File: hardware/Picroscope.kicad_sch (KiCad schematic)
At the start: 34 parts, among them J1 USB_C_Receptacle_USB2.0_16P, J2 Conn_01x03_Pin, J3 HDMI_A, J4 Conn_02x09_Odd_Even, U3 AMS1117-3.3

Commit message: added length tuning to 'crucial' traces except qspi
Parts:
- D2: footprint LED_SMD:LED_WS2812B-2020_PLCC4_2.0x2.0mm -> LED_SMD:LED_WS2812B_PLCC4_5.0x5.0mm_P3.2mm
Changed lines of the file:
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@@
 			)
 		)
-		(property "Footprint" "LED_SMD:LED_WS2812B-2020_PLCC4_2.0x2.0mm"
+		(property "Footprint" "LED_SMD:LED_WS2812B_PLCC4_5.0x5.0mm_P3.2mm"
 			(at 87.63 179.07 0)
 			(effects

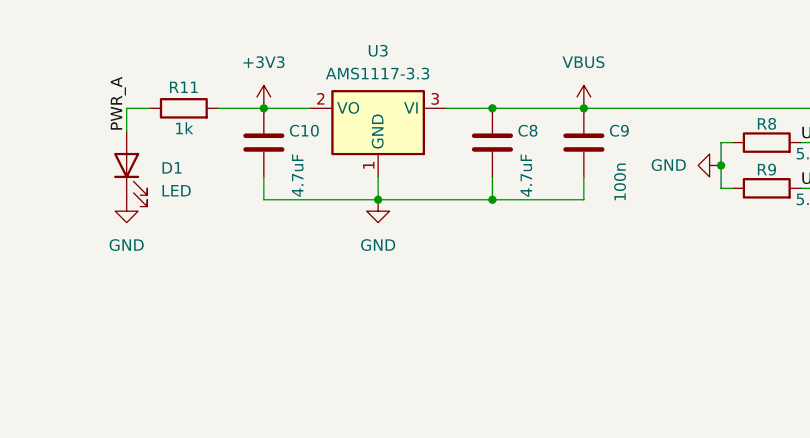
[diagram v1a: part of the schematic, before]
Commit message: changed C8 & C10 to tantalum caps
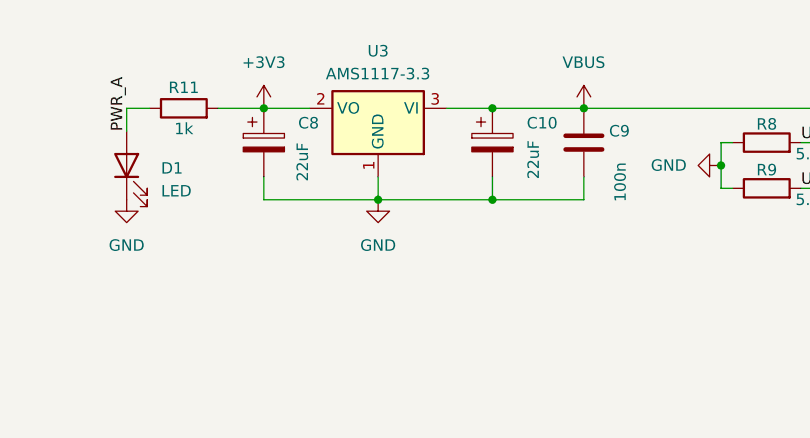
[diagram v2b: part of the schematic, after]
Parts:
- removed C10, C8: 4.7uF, Capacitor_SMD:C_0402_1005Metric, symbol Device:C
- added C10, C8: 22uF, Capacitor_Tantalum_SMD:CP_EIA-3216-18_Kemet-A, symbol Device:C_Polarized
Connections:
- net +3V3: now also C8.1
- net GND: now also C10.2, C8.2
- net VBUS: now also C10.1
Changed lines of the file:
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@@
 	(paper "A4")
 	(junction
-		(at 177.8 30.48)
-		(diameter 0)
-		(color 0 0 0 0)
-	)
-	(junction
 		(at 241.3 96.52)
 		(diameter 0)
@@
 	)
 	(junction
+		(at 177.8 30.48)
+		(diameter 0)
+		(color 0 0 0 0)
+	)
+	(junction
 		(at 39.37 124.46)
 		(diameter 0)
@@
 	(wire
 		(pts
+			(xy 177.8 30.48) (xy 187.96 30.48)
+		)
+		(stroke
+			(width 0)
+			(type default)
+		)
+	)
+	(wire
+		(pts
 			(xy 129.54 104.14) (xy 129.54 105.41)
 		)
@@
 	(wire
 		(pts
-			(xy 177.8 30.48) (xy 187.96 30.48)
-		)
-		(stroke
-			(width 0)
-			(type default)
-		)
-	)
-	(wire
-		(pts
 			(xy 53.34 107.95) (xy 66.04 107.95)
 		)
@@
 	)
 	(symbol
+		(lib_id "Device:C_Polarized")
+		(at 177.8 34.29 0)
+		(unit 1)
+		(exclude_from_sim no)
+		(in_bom yes)
+		(on_board yes)
+		(dnp no)
+		(property "Reference" "C10"
+			(at 181.61 32.1309 0)
+			(effects
+				(font
+					(size 1.27 1.27)
+				)
+				(justify left)
+			)
+		)
+		(property "Value" "22uF"
+			(at 182.372 38.354 90)
+			(effects
+				(font
+					(size 1.27 1.27)
+				)
+				(justify left)
+			)
+		)
+		(property "Footprint" "Capacitor_Tantalum_SMD:CP_EIA-3216-18_Kemet-A"
+			(at 178.7652 38.1 0)
+			(effects
+				(font
+					(size 1.27 1.27)
+				)
+				(hide yes)
+			)
+		)
+		(property "Datasheet" "~"
+			(at 177.8 34.29 0)
+			(effects
+				(font
+					(size 1.27 1.27)
+				)
+				(hide yes)
+			)
+		)
+		(property "Description" "Polarized capacitor"
+			(at 177.8 34.29 0)
+			(effects
+				(font
+					(size 1.27 1.27)
+				)
+				(hide yes)
+			)
+		)
+		(pin "1"
+		)
+		(pin "2"
+		)
+		(instances
+			(project ""
+				(path "/7331d441-a240-49c5-9321-48c59c370619"
+					(reference "C10")
+					(unit 1)
+				)
+			)
+		)
+	)
+	(symbol
 		(lib_id "Mechanical:MountingHole")
 		(at 20.32 166.37 0)
@@
 	)
 	(symbol
-		(lib_id "Device:C")
-		(at 152.4 34.29 0)
-		(unit 1)
-		(exclude_from_sim no)
-		(in_bom yes)
-		(on_board yes)
-		(dnp no)
-		(property "Reference" "C10"
-			(at 155.194 33.02 0)
-			(effects
-				(font
-					(size 1.27 1.27)
-				)
-				(justify left)
-			)
-		)
-		(property "Value" "4.7uF"
-			(at 156.21 40.386 90)
-			(effects
-				(font
-					(size 1.27 1.27)
-				)
-				(justify left)
-			)
-		)
-		(property "Footprint" "Capacitor_SMD:C_0402_1005Metric"
-			(at 153.3652 38.1 0)
-			(effects
-				(font
-					(size 1.27 1.27)
-				)
-				(hide yes)
-			)
-		)
-		(property "Datasheet" "~"
-			(at 152.4 34.29 0)
-			(effects
-				(font
-					(size 1.27 1.27)
-				)
-				(hide yes)
-			)
-		)
-		(property "Description" "Unpolarized capacitor"
-			(at 152.4 34.29 0)
-			(effects
-				(font
-					(size 1.27 1.27)
-				)
-				(hide yes)
-			)
-		)
-		(pin "1"
-		)
-		(pin "2"
-		)
-		(instances
-			(project "Picroscope"
-				(path "/7331d441-a240-49c5-9321-48c59c370619"
-					(reference "C10")
-					(unit 1)
-				)
-			)
-		)
-	)
-	(symbol
 		(lib_id "Connector:TestPoint")
 		(at 220.98 39.37 270)
@@
 	)
 	(symbol
-		(lib_id "Device:C")
-		(at 177.8 34.29 0)
-		(unit 1)
-		(exclude_from_sim no)
-		(in_bom yes)
-		(on_board yes)
-		(dnp no)
-		(property "Reference" "C8"
-			(at 180.594 33.02 0)
-			(effects
-				(font
-					(size 1.27 1.27)
-				)
-				(justify left)
-			)
-		)
-		(property "Value" "4.7uF"
-			(at 181.61 40.386 90)
-			(effects
-				(font
-					(size 1.27 1.27)
-				)
-				(justify left)
-			)
-		)
-		(property "Footprint" "Capacitor_SMD:C_0402_1005Metric"
-			(at 178.7652 38.1 0)
-			(effects
-				(font
-					(size 1.27 1.27)
-				)
-				(hide yes)
-			)
-		)
-		(property "Datasheet" "~"
-			(at 177.8 34.29 0)
-			(effects
-				(font
-					(size 1.27 1.27)
-				)
-				(hide yes)
-			)
-		)
-		(property "Description" "Unpolarized capacitor"
-			(at 177.8 34.29 0)
-			(effects
-				(font
-					(size 1.27 1.27)
-				)
-				(hide yes)
-			)
-		)
-		(pin "1"
-		)
-		(pin "2"
-		)
-		(instances
-			(project ""
-				(path "/7331d441-a240-49c5-9321-48c59c370619"
-					(reference "C8")
-					(unit 1)
-				)
-			)
-		)
-	)
-	(symbol
 		(lib_id "power:GND")
 		(at 243.84 156.21 0)
@@
 					(unit 1)
 				)
+			)
+		)
+	)
+	(symbol
+		(lib_id "Device:C_Polarized")
+		(at 152.4 34.29 0)
+		(unit 1)
+		(exclude_from_sim no)
+		(in_bom yes)
+		(on_board yes)
+		(dnp no)
+		(property "Reference" "C8"
+			(at 156.21 32.1309 0)
+			(effects
+				(font
+					(size 1.27 1.27)
+				)
+				(justify left)
+			)
+		)
+		(property "Value" "22uF"
+			(at 156.718 38.608 90)
+			(effects
+				(font
+					(size 1.27 1.27)
+				)
+				(justify left)
+			)
+		)
+		(property "Footprint" "Capacitor_Tantalum_SMD:CP_EIA-3216-18_Kemet-A"
+			(at 153.3652 38.1 0)
+			(effects
+				(font
+					(size 1.27 1.27)
+				)
+				(hide yes)
+			)
+		)
+		(property "Datasheet" "~"
+			(at 152.4 34.29 0)
+			(effects
+				(font
+					(size 1.27 1.27)
+				)
+				(hide yes)
+			)
+		)
+		(property "Description" "Polarized capacitor"
+			(at 152.4 34.29 0)
+			(effects
+				(font
+					(size 1.27 1.27)
+				)
+				(hide yes)
+			)
+		)
+		(pin "1"
+		)
+		(pin "2"
+		)
+		(instances
+			(project ""
+				(path "/7331d441-a240-49c5-9321-48c59c370619"
+					(reference "C8")
+					(unit 1)
+				)

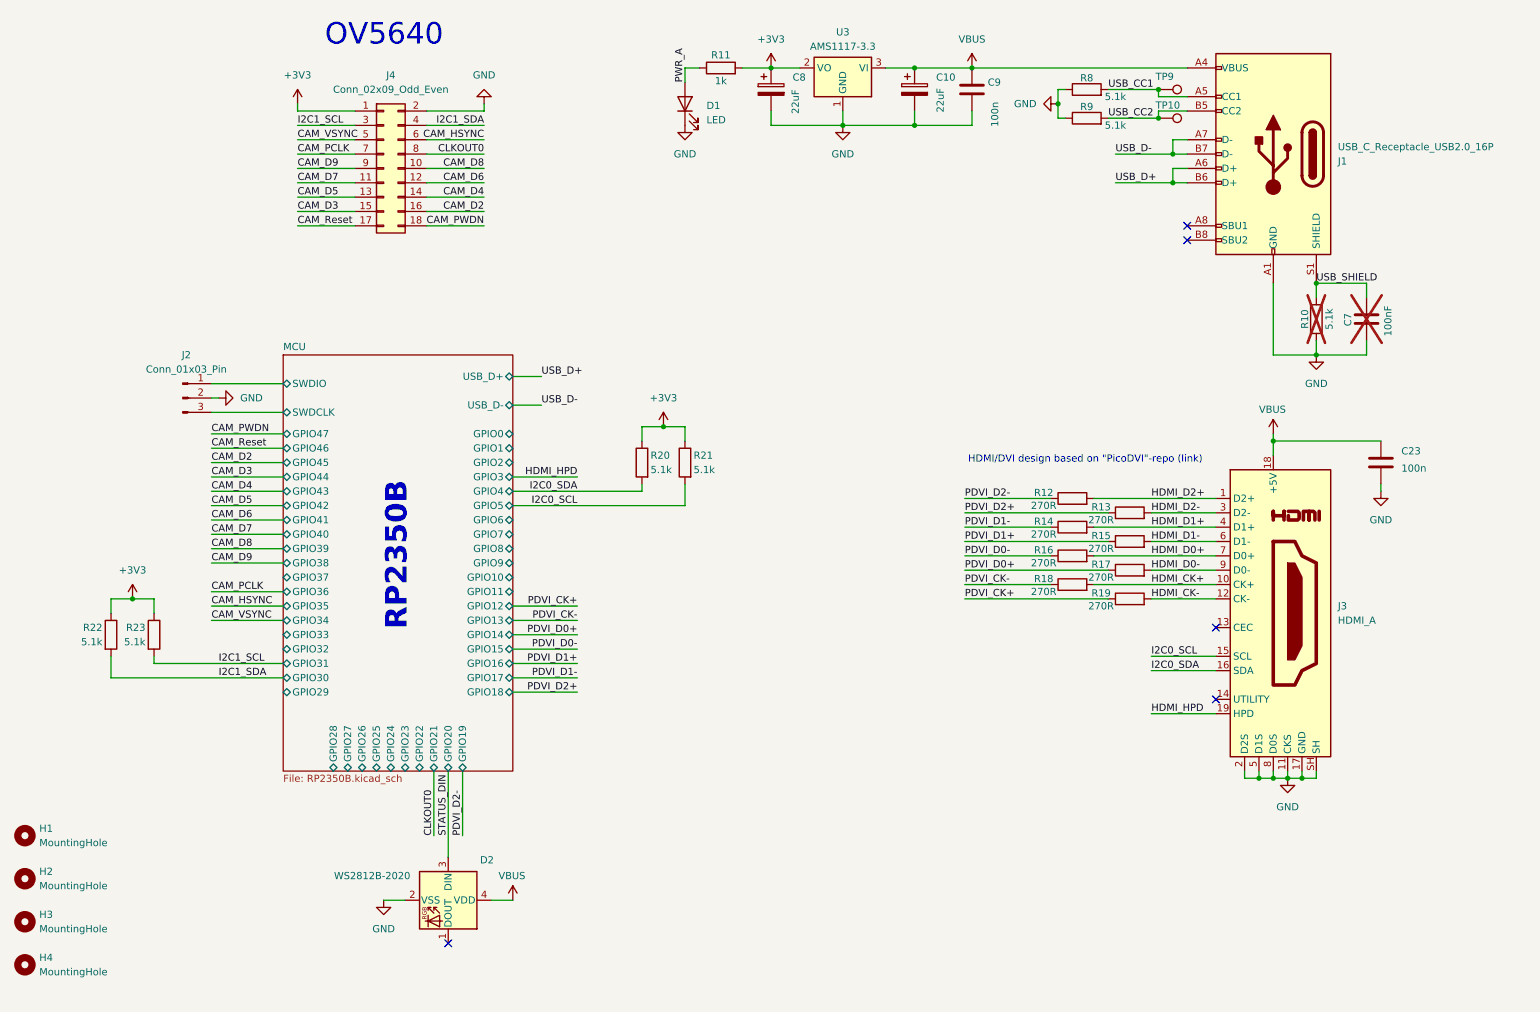
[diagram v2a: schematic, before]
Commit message: fixed short to GND on CLKOUT0
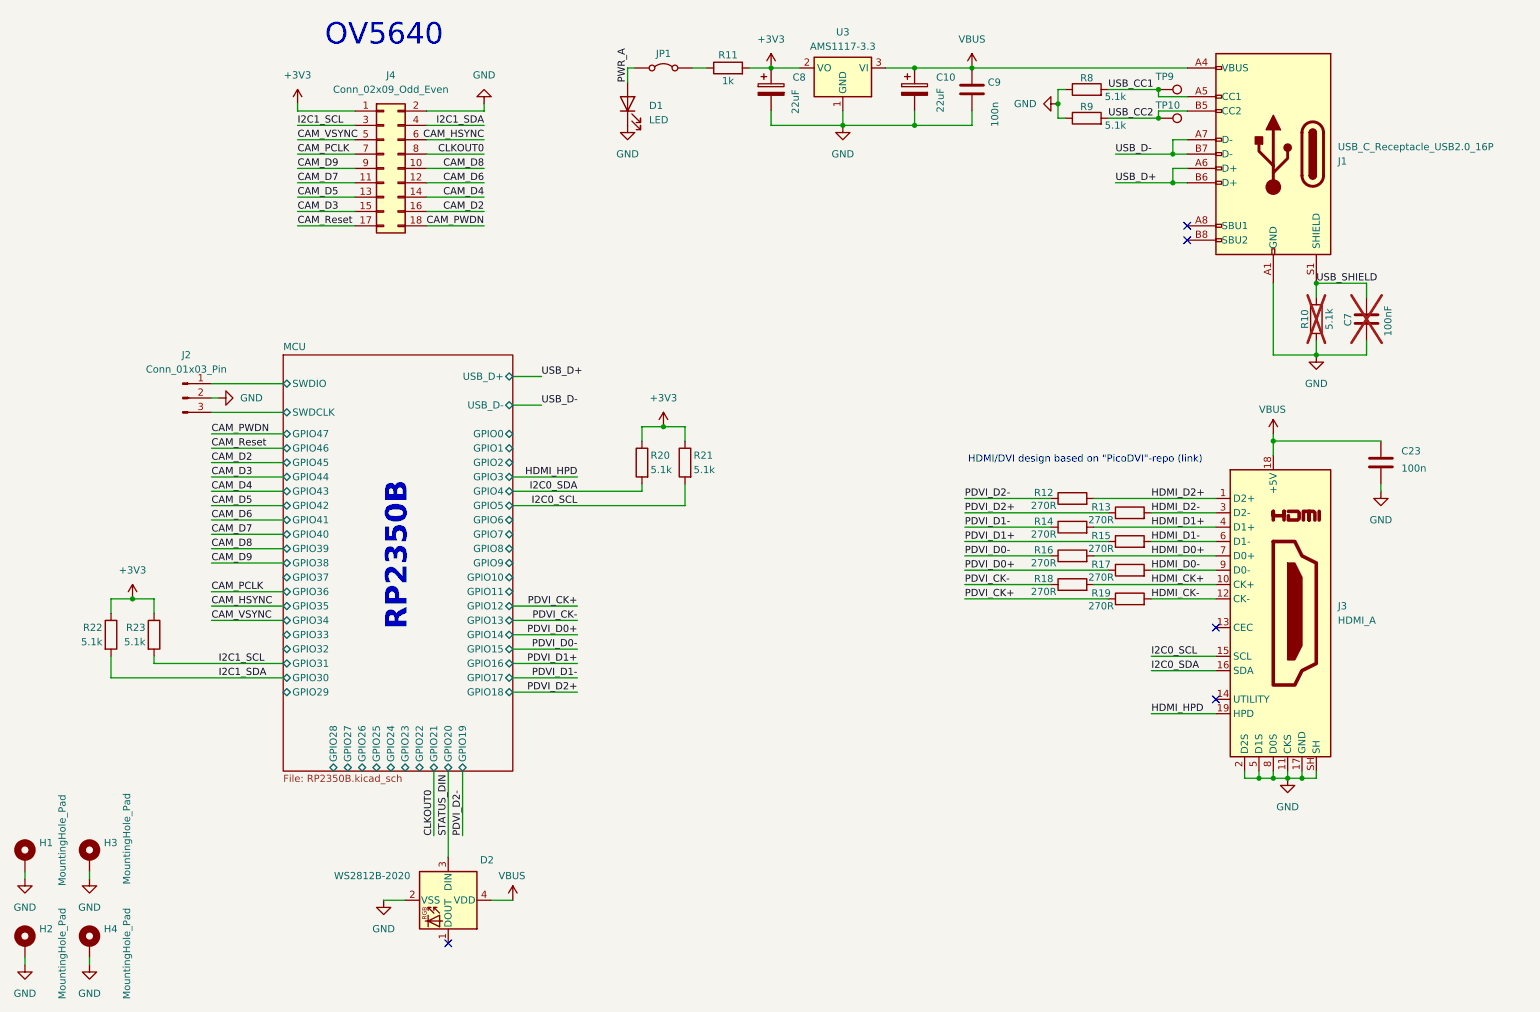
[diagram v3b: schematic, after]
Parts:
- removed H1, H2, H3, H4: MountingHole, MountingHole:MountingHole_3.2mm_M3_DIN965, symbol Mechanical:MountingHole
- added H1, H2, H3, H4: MountingHole_Pad, MountingHole:MountingHole_3.2mm_M3_DIN965_Pad_TopBottom, symbol Mechanical:MountingHole_Pad
- added JP1: Jumper_2_Bridged, Jumper:SolderJumper-2_P1.3mm_Bridged_RoundedPad1.0x1.5mm, symbol Jumper:Jumper_2_Bridged
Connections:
- net GND: now also H1.1, H2.1, H3.1, H4.1
- net PWR_A: now also JP1.1 (A); no longer R11.1
- new net: JP1.2 (B), R11.1
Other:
- company: (none) -> Nico Zehetner
- title: (none) -> PIcroscope - A RP2350 based Microscope
- moved on the sheet: D1
